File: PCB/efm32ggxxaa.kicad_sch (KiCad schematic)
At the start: 11 parts, among them J102 EFM32_PinHeader_PortE, U5 EFM32GG11B420F2048GQ100, Y101 72MHz

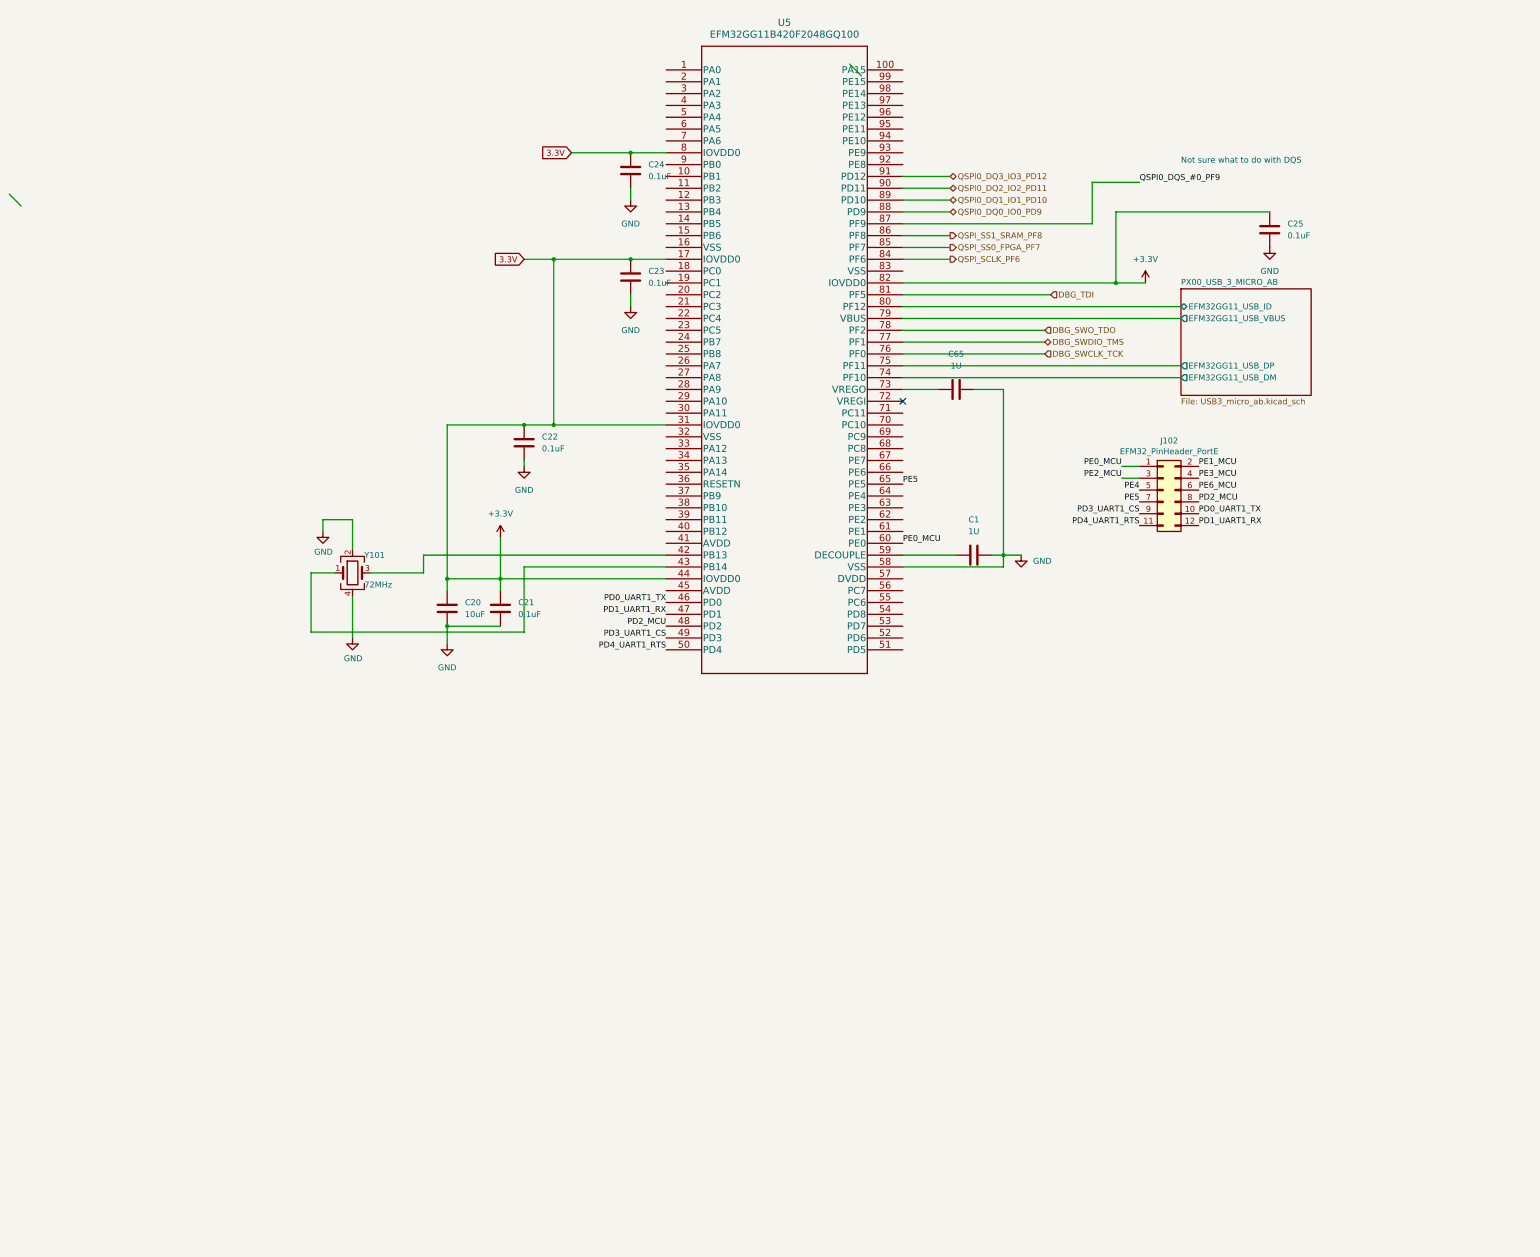
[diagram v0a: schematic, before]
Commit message: Clean up MCU ++
Signed-off-by: Daniel Yang Hansen <daniel.yang.hansen@gmail.com>
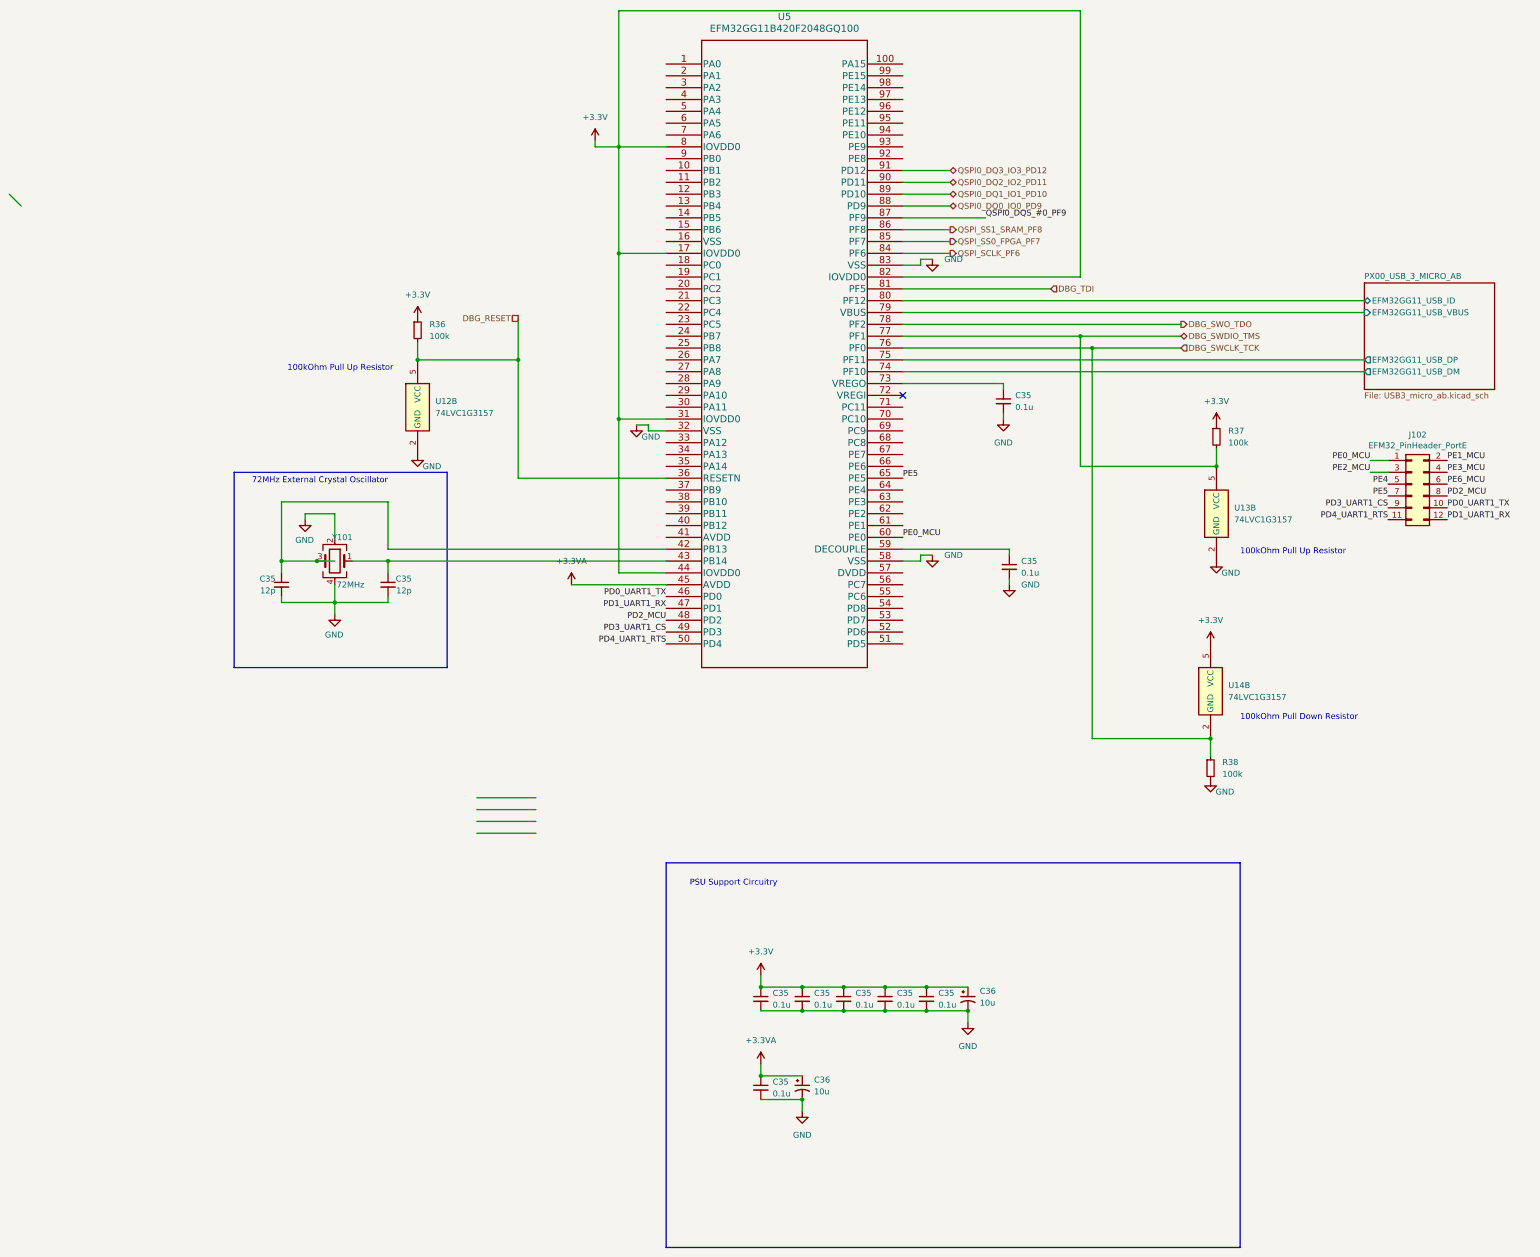
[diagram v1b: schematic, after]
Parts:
- removed C1, C65: 1U, symbol Device:C
- removed C20: 10uF, symbol Device:C
- removed C21, C22, C23, C24, C25: 0.1uF, symbol Device:C
- added C35 (x8): 0.1u, symbol Device:C_Small
- added C35 (x2): 12p, symbol Device:C_Small
- added C36 (x2): 10u, symbol Device:C_Polarized_Small_US
- added R36, R37, R38: 100k, symbol Device:R_Small
- added U12, U13, U14: 74LVC1G3157, symbol 74xGxx:74LVC1G3157
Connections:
- net +3.3V: now also C35.1, C35.1, C35.1, C35.1, C35.1, C36.1, R36.1, R37.1, U14.5 (VCC)
- net DBG_SWCLK_TCK: now also R38.1, U14.2 (GND)
- net DBG_SWDIO_TMS: now also R37.2, U13.5 (VCC)
- net GND: now also U5.32 (VSS), U5.83 (VSS), C35.2, C35.2, C35.2, C35.2, C35.2, C35.2, C35.2, C35.2, C35.2, C35.2, C36.2, C36.2, R38.2, U12.2 (GND), U13.2 (GND)
- net at U5.73 (VREGO): now also C35.1
- net at U5.59 (DECOUPLE): now also C35.1
- net DBG_RESET: now reaches U5.36 (RESETN)
- net DBG_RESET: now also R36.2, U12.5 (VCC)
- net at U5.42 (PB13), Y101.3: now also C35.1
- net at U5.43 (PB14), Y101.1: now also C35.1
- net +3.3VA: now reaches U5.45 (AVDD)
- net +3.3VA: now also C35.1, C36.1
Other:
- note added: "100kOhm Pull Down Resistor"
- note added: "100kOhm Pull Up Resistor"
- note added: "72MHz External Crystal Oscillator"
- note added: "PSU Support Circuitry"
- note removed: "Not sure what to do with DQS"
- moved on the sheet: J102, U5, Y101
